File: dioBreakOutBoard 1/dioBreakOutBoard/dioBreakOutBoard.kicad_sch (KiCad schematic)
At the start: 7 parts

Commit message: C:\Users\khernandez\KiCad\KiCad-Projects# Please enter the commit message for your changes. Lines starting
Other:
- removed sheet HPC DIO Header
- removed sheet LPC DIO Header
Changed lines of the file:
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@@
 	)
 	(sheet
-		(at 189.23 127)
+		(at 133.35 124.46)
 		(size 12.7 19.05)
 		(fields_autoplaced yes)
@@
 		)
 		(property "Sheetname" "BUFFERS1"
-			(at 189.23 126.2884 0)
+			(at 133.35 123.7484 0)
 			(effects
 				(font
@@
 		)
 		(property "Sheetfile" "BUFFERS_cont.kicad_sch"
-			(at 189.23 146.6346 0)
+			(at 133.35 144.0946 0)
 			(effects
 				(font
@@
 	)
 	(sheet
-		(at 153.67 62.23)
-		(size 20.32 44.45)
-		(fields_autoplaced yes)
-		(stroke
-			(width 0.1524)
-			(type solid)
-		)
-		(fill
-			(color 0 0 0 0.0000)
-		)
-		(property "Sheetname" "HPC DIO Header"
-			(at 153.67 61.5184 0)
-			(effects
-				(font
-					(size 1.27 1.27)
-				)
-				(justify left bottom)
-			)
-		)
-		(property "Sheetfile" "FMC0_DIO_Header.kicad_sch"
-			(at 153.67 107.2646 0)
-			(effects
-				(font
-					(size 1.27 1.27)
-				)
-				(justify left top)
-			)
-		)
-		(instances
-			(project "dioBreakOutBoard"
-				(path "/98e3a74d-079b-42d2-b386-3e452c68576a"
-					(page "8")
-				)
-			)
-		)
-	)
-	(sheet
-		(at 204.47 59.69)
+		(at 106.68 60.96)
 		(size 41.91 48.26)
 		(fields_autoplaced yes)
@@
 		)
 		(property "Sheetname" "VME_BREAKOUT"
-			(at 204.47 58.9784 0)
+			(at 106.68 60.2484 0)
 			(effects
 				(font
@@
 		)
 		(property "Sheetfile" "VME_BRKOUT.kicad_sch"
-			(at 204.47 108.5346 0)
+			(at 106.68 109.8046 0)
 			(effects
 				(font
@@
 	)
 	(sheet
-		(at 162.56 127)
+		(at 106.68 124.46)
 		(size 12.7 19.05)
 		(fields_autoplaced yes)
@@
 		)
 		(property "Sheetname" "BUFFERS"
-			(at 162.56 126.2884 0)
+			(at 106.68 123.7484 0)
 			(effects
 				(font
@@
 		)
 		(property "Sheetfile" "BUFFERS.kicad_sch"
-			(at 162.56 146.6346 0)
+			(at 106.68 144.0946 0)
 			(effects
 				(font
@@
 				)
 			)
-		)
-	)
-	(sheet
-		(at 152.4 175.26)
-		(size 19.05 34.29)
-		(fields_autoplaced yes)
-		(stroke
-			(width 0.1524)
-			(type solid)
-		)
-		(fill
-			(color 0 0 0 0.0000)
-		)
-		(property "Sheetname" "LPC DIO Header"
-			(at 152.4 174.5484 0)
-			(effects
-				(font
-					(size 1.27 1.27)
-				)
-				(justify left bottom)
-			)
-		)
-		(property "Sheetfile" "LPC_DIO_Header.kicad_sch"
-			(at 152.4 210.1346 0)
-			(effects
-				(font
-					(size 1.27 1.27)
-				)
-				(justify left top)
-			)
-		)
-		(instances
-			(project "dioBreakOutBoard"
-				(path "/98e3a74d-079b-42d2-b386-3e452c68576a"
-					(page "9")
-				)
-			)

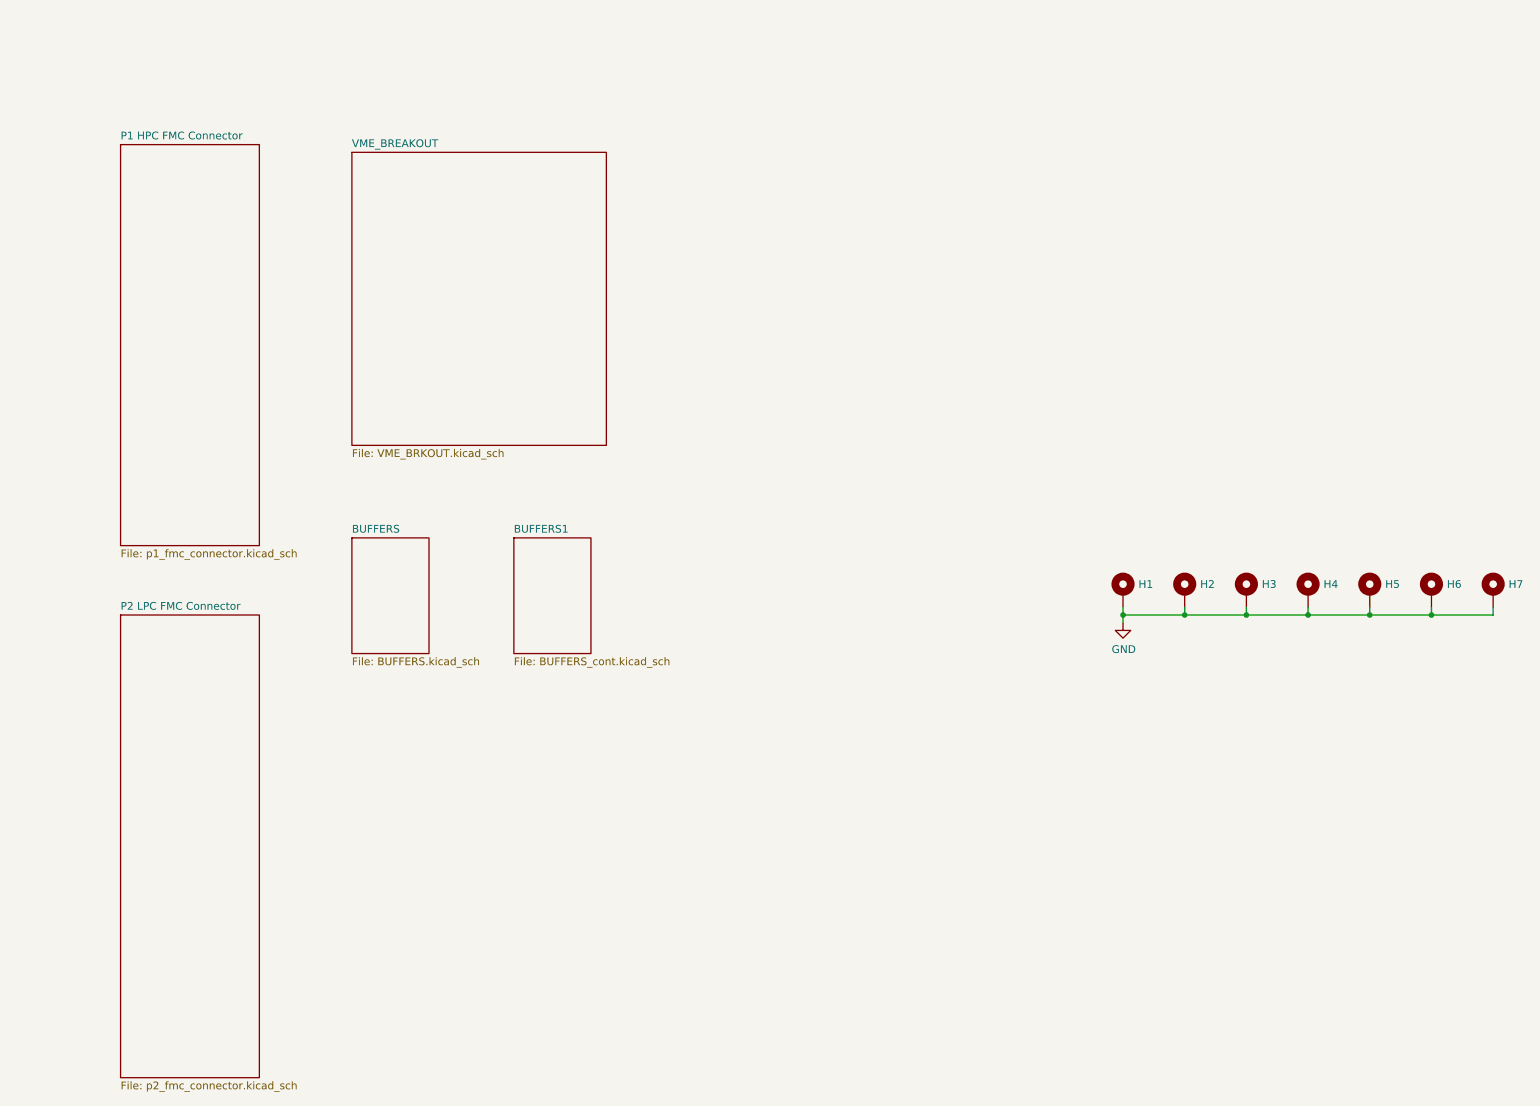
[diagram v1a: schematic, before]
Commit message: added 2 bit buffers, which replace the previous 8 bit buffers
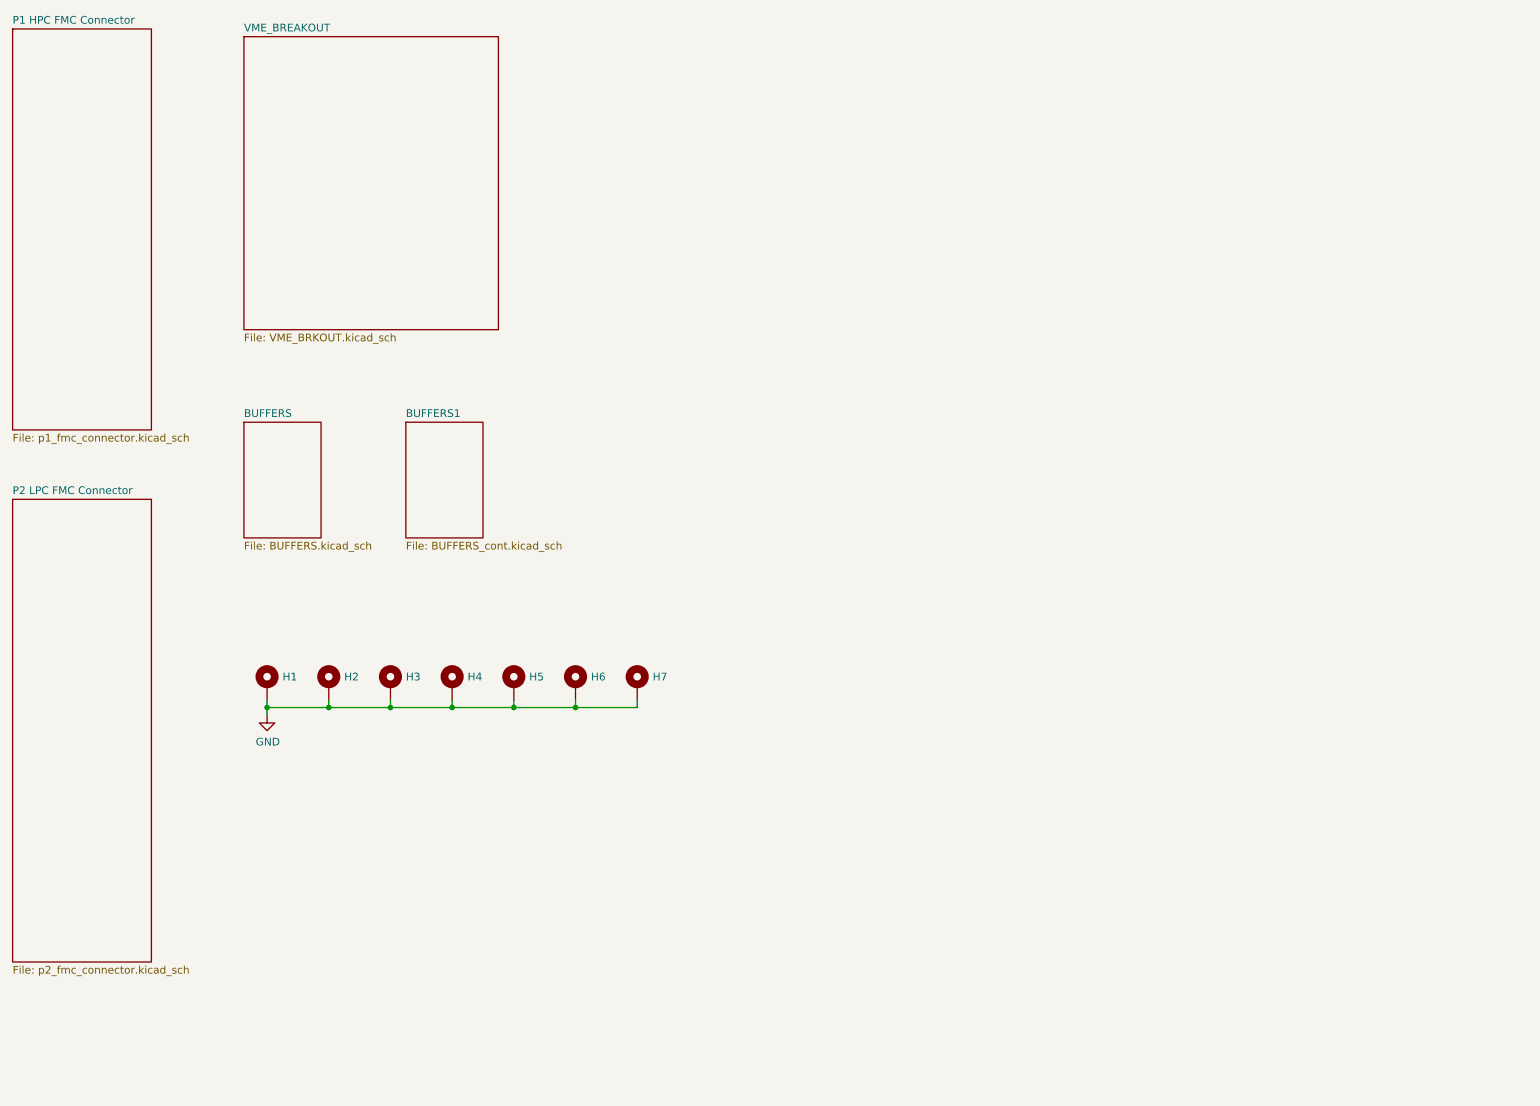
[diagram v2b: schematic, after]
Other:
- moved on the sheet: H1, H2, H3, H4, H5, H6, H7
